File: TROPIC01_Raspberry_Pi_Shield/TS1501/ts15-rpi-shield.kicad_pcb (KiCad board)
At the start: 2 copper layers, 56 x 65 mm, 14 parts, among them CON1 TROPIC01, IC1 TROPIC01_chip, J1 RPI socket, J2 CS select jumper switch

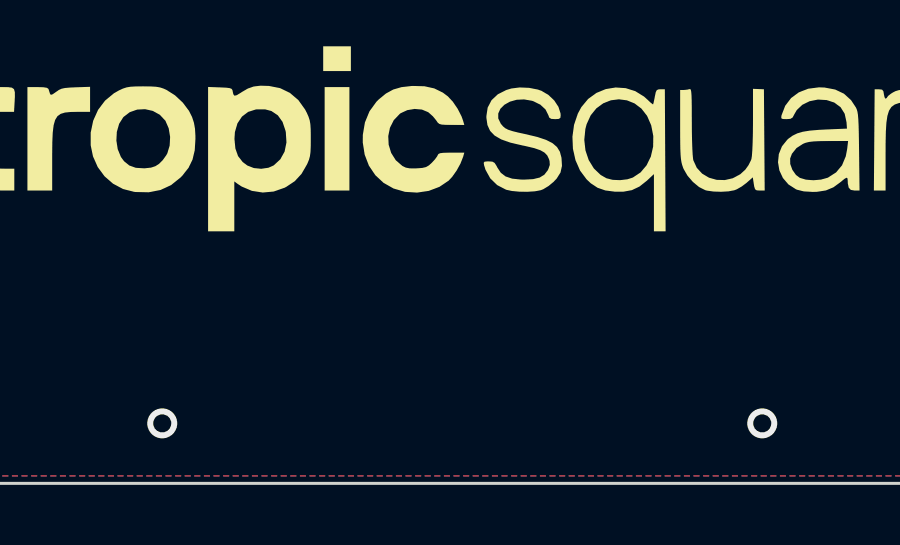
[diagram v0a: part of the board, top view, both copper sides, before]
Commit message: feat: Add Silkscreen rectangle to TS1501
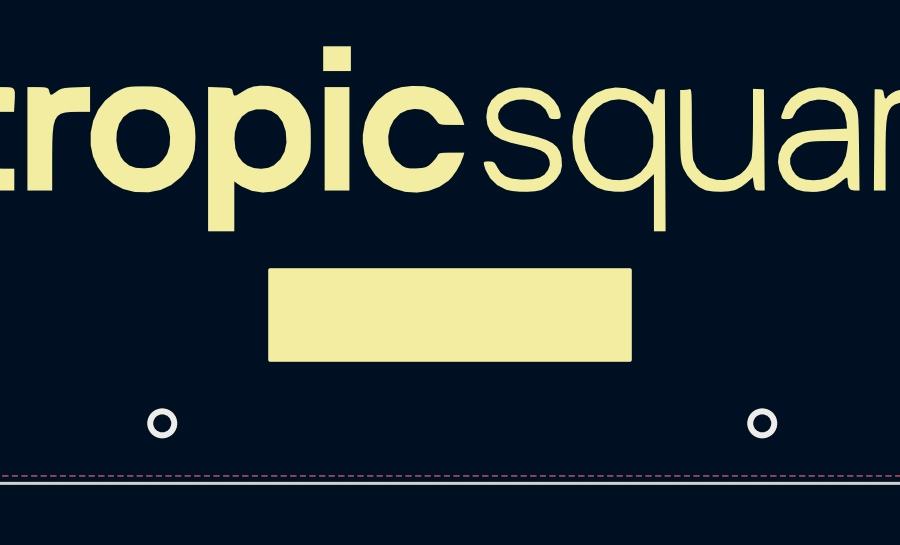
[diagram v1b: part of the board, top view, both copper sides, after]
